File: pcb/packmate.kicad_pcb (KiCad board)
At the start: 2 copper layers, 77.2 x 93.3 mm, 49 parts, among them J2 DISPLAY, J7 MICROSD, Q1 2N7002E, SW1 BTN, SW2 Reset Button, SW3 Left Button, SW4 Right Button, SW6 Wireless On/Off Switch, U1 UP, U2 DWN, U3 LFT, U4 RHT

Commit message: Still tidying pcb design
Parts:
- removed C2: 0.1uf, Capacitor_SMD:C_01005_0402Metric
- added C10: 100nF, Capacitor_SMD:C_0402_1005Metric, B.Cu at (74.6, 70.3)
- added C11: 100nF, Capacitor_SMD:C_0402_1005Metric, B.Cu at (66.4, 114.6)
- added C12: 100nF, Capacitor_SMD:C_0402_1005Metric, B.Cu at (66.8, 127.0)
- added C13: 100nF, Capacitor_SMD:C_0402_1005Metric, B.Cu at (66.6, 140.1)
- added C14: 100nF, Capacitor_SMD:C_0402_1005Metric, B.Cu at (139.1, 127.3)
- added C15: 100nF, Capacitor_SMD:C_0402_1005Metric, B.Cu at (138.5, 115.9)
- added C16: 100nF, Capacitor_SMD:C_0402_1005Metric, B.Cu at (139.5, 104.5)
- added C17: 100nF, Capacitor_SMD:C_0402_1005Metric, B.Cu at (139.0, 79.2)
- added C18: 100nF, Capacitor_SMD:C_0402_1005Metric, B.Cu at (126.4, 69.6)
- added C9: 100nF, Capacitor_SMD:C_0402_1005Metric, B.Cu at (83.3, 66.1)
- added R13: 100, Resistor_SMD:R_0603_1608Metric, B.Cu at (116.9, 95.3)
- C1: footprint Capacitor_SMD:C_01005_0402Metric -> Capacitor_SMD:C_0402_1005Metric
- C3: value 400uf -> 100uf; footprint Capacitor_SMD:CP_Elec_3x5.3 -> Capacitor_SMD:CP_Elec_4x5.4
- C8: footprint Capacitor_SMD:C_01005_0402Metric -> Capacitor_SMD:C_0402_1005Metric; moved to B.Cu
- R10, R11, R12: footprint Resistor_SMD:R_0201_0603Metric -> Resistor_SMD:R_0603_1608Metric
- R9: value 10 -> 180; footprint Resistor_SMD:R_0201_0603Metric -> Resistor_SMD:R_0603_1608Metric
- moved R10 3.20 mm to (106.7, 91.5)
- moved R9 2.48 mm to (90.4, 92.9), turned to 180 degrees
- moved C8 1.82 mm to (86.0, 101.2)
- moved C1 1.27 mm to (99.7, 99.2), turned to 0 degrees
- moved R12 1.24 mm to (83.2, 101.5)
- moved Q1 1.22 mm to (108.1, 87.9), turned to -90 degrees
- moved D7 0.94 mm to (72.8, 74.5)
- moved R11 0.94 mm to (83.2, 98.6), turned to 0 degrees
- moved C3 0.30 mm to (88.9, 64.6)
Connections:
- net /3v3 renamed /3V3
- net /5v renamed /VSYS
- A1 pad 33: unconnected-(A1-AGND-Pad33) -> GND
- BZ1 pad 1: Net-(A1-GPIO12) -> Net-(BZ1-+)
- Q1 pad 2: Net-(Q1-S) -> /Display Connector/GND
- Q1 pad 3: /Display Connector/GND -> Net-(Q1-D)
- R10 pad 1: Net-(Q1-S) -> Net-(Q1-D)
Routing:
- net /Display Connector/GND: track 622.8 -> 111.7 mm, vias 9 -> 3
- net /VSYS: track 273.7 -> 284.4 mm
- net Net-(A1-RUN): track 121.6 -> 115.8 mm
- net Net-(BZ1-+): track 0.00 -> 5.64 mm
- net Net-(A1-GPIO12): track 8.73 -> 4.51 mm
- net /Display Connector/LEDK: track 8.69 -> 4.77 mm
- net Net-(A1-GPIO21): track 8.19 -> 5.13 mm
- net /3V3: track 195.9 -> 193.2 mm
- net Net-(Q1-D): track 0.00 -> 2.40 mm
- net Net-(A1-GPIO13): track 14.6 -> 16.2 mm
- net Net-(Q1-S): track 1.23 -> 0.00 mm
- net Net-(D5-A): track 2.26 -> 3.49 mm
- net /Display Connector/CS: track 22.2 -> 21.3 mm
- net /Display Connector/D/C: track 22.7 -> 21.7 mm
- net /Display Connector/SCL: track 17.2 -> 16.4 mm
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- added copper zone on B.Cu, net /Display Connector/GND
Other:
- outline, holes or cut-outs redrawn

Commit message: Still improving pcb, I learned what a fiducial is today
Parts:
- added REF**: Fiducial_1mm_Mask2mm, Fiducial:Fiducial_1mm_Mask2mm, F.Cu at (135.2, 72.0)
- added REF**: Fiducial_1mm_Mask2mm, Fiducial:Fiducial_1mm_Mask2mm, F.Cu at (73.5, 83.0)
- added REF**: Fiducial_1mm_Mask2mm, Fiducial:Fiducial_1mm_Mask2mm, F.Cu at (138.5, 131.8)
- added REF**: Fiducial_1mm_Mask2mm, Fiducial:Fiducial_1mm_Mask2mm, B.Cu at (73.5, 83.0)
- added REF**: Fiducial_1mm_Mask2mm, Fiducial:Fiducial_1mm_Mask2mm, B.Cu at (135.2, 72.0)
- added REF**: Fiducial_1mm_Mask2mm, Fiducial:Fiducial_1mm_Mask2mm, B.Cu at (138.5, 131.8)
- C8: moved to F.Cu
- moved SW3 8.08 mm to (88.0, 138.2), turned to 180 degrees
- moved C9 1.14 mm to (82.5, 65.2)
- moved C16 1.05 mm to (138.5, 104.8)
- moved C10 0.88 mm to (75.3, 69.8)
- moved C8 0.87 mm to (85.2, 100.8)
- moved C11 0.49 mm to (66.8, 114.2)
- moved C14 0.45 mm to (139.1, 127.8)
- moved Q1 0.32 mm to (107.8, 87.8)
- moved R10 0.18 mm to (106.8, 91.3)
- moved C3 0.18 mm to (88.8, 64.5)
- moved R12 0.11 mm to (83.2, 101.6)
- moved C1 0.06 mm to (99.8, 99.2)
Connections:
- net /3V3 renamed +3.3V
- net /VSYS renamed VSYS
- A1 pad 13: /Display Connector/GND -> GND
- A1 pad 17: Net-(A1-GPIO13) -> /Display Connector/LEDK
- A1 pad 18: /Display Connector/GND -> GND
- A1 pad 23: /Display Connector/GND -> GND
- A1 pad 28: /Display Connector/GND -> GND
- A1 pad 3: /Display Connector/GND -> GND
- A1 pad 38: /Display Connector/GND -> GND
- A1 pad 8: /Display Connector/GND -> GND
- BZ1 pad 2: /Display Connector/GND -> GND
- C1 pad 1: /Display Connector/GND -> GND
- C10 pad 1: /Display Connector/GND -> GND
- C11 pad 1: /Display Connector/GND -> GND
- C12 pad 1: /Display Connector/GND -> GND
- C13 pad 1: /Display Connector/GND -> GND
- C14 pad 1: /Display Connector/GND -> GND
- C15 pad 1: /Display Connector/GND -> GND
- C16 pad 1: /Display Connector/GND -> GND
- C17 pad 1: /Display Connector/GND -> GND
- C18 pad 1: /Display Connector/GND -> GND
- C3 pad 2: /Display Connector/GND -> GND
- C4 pad 2: /Display Connector/GND -> GND
- C5 pad 2: /Display Connector/GND -> GND
- C6 pad 2: /Display Connector/GND -> GND
- C7 pad 2: /Display Connector/GND -> GND
- C8 pad 1: /Display Connector/GND -> GND
- C9 pad 1: /Display Connector/GND -> GND
- D1 pad 1: /Display Connector/GND -> GND
- D10 pad 3: /Display Connector/GND -> GND
- D11 pad 3: /Display Connector/GND -> GND
- D12 pad 3: /Display Connector/GND -> GND
- D13 pad 3: /Display Connector/GND -> GND
- D14 pad 3: /Display Connector/GND -> GND
- D15 pad 3: /Display Connector/GND -> GND
- D2 pad 1: /Display Connector/GND -> GND
- D3 pad 1: /Display Connector/GND -> GND
- D4 pad 1: /Display Connector/GND -> GND
- D5 pad 1: /Display Connector/GND -> GND
- D6 pad 3: /Display Connector/GND -> GND
- D7 pad 3: /Display Connector/GND -> GND
- D8 pad 3: /Display Connector/GND -> GND
- D9 pad 3: /Display Connector/GND -> GND
- J2 pad 1: /Display Connector/GND -> GND
- J2 pad 12: /Display Connector/GND -> GND
- J2 pad 2: /Display Connector/LEDK -> Net-(J2-Pin_2)
- J2 pad 5: /Display Connector/GND -> GND
- J2 pad 6: /Display Connector/GND -> GND
- J2 pad MP: (no net) -> GND
- J7 pad 6: /Display Connector/GND -> GND
- Q1 pad 1: Net-(A1-GPIO13) -> /Display Connector/LEDK
- Q1 pad 2: /Display Connector/GND -> GND
- R10 pad 2: /Display Connector/LEDK -> Net-(J2-Pin_2)
- SW1 pad 1: /Display Connector/GND -> GND
- SW2 pad 1: /Display Connector/GND -> GND
- SW3 pad 1: /Display Connector/GND -> GND
- SW4 pad 1: /Display Connector/GND -> GND
- SW6 pad 1: /Display Connector/GND -> GND
- U1 pad 3: /Display Connector/GND -> GND
- U2 pad 3: /Display Connector/GND -> GND
- U3 pad 3: /Display Connector/GND -> GND
- U4 pad 3: /Display Connector/GND -> GND
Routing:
- net GND: track 0.00 -> 121.5 mm, vias 0 -> 5
- net /Display Connector/GND: track 111.7 -> 0.00 mm, vias 3 -> 0
- net Net-(A1-GPIO15): track 92.5 -> 75.2 mm
- net Net-(A1-GPIO13): track 16.2 -> 0.00 mm
- net /Display Connector/LEDK: track 4.77 -> 16.4 mm, vias 1 -> 0
- net VSYS: track 284.4 -> 289.6 mm
- net Net-(J2-Pin_2): track 0.00 -> 4.77 mm, vias 0 -> 1
- net Net-(A1-GPIO14): track 54.7 -> 50.4 mm
- net Net-(D7-DOUT): track 54.4 -> 55.1 mm
- net /Trackball/BTN: track 82.1 -> 82.8 mm
- net Net-(D10-DOUT): track 91.9 -> 92.5 mm
- added copper zone on B.Cu, net GND
- removed copper zone on B.Cu, net /Display Connector/GND

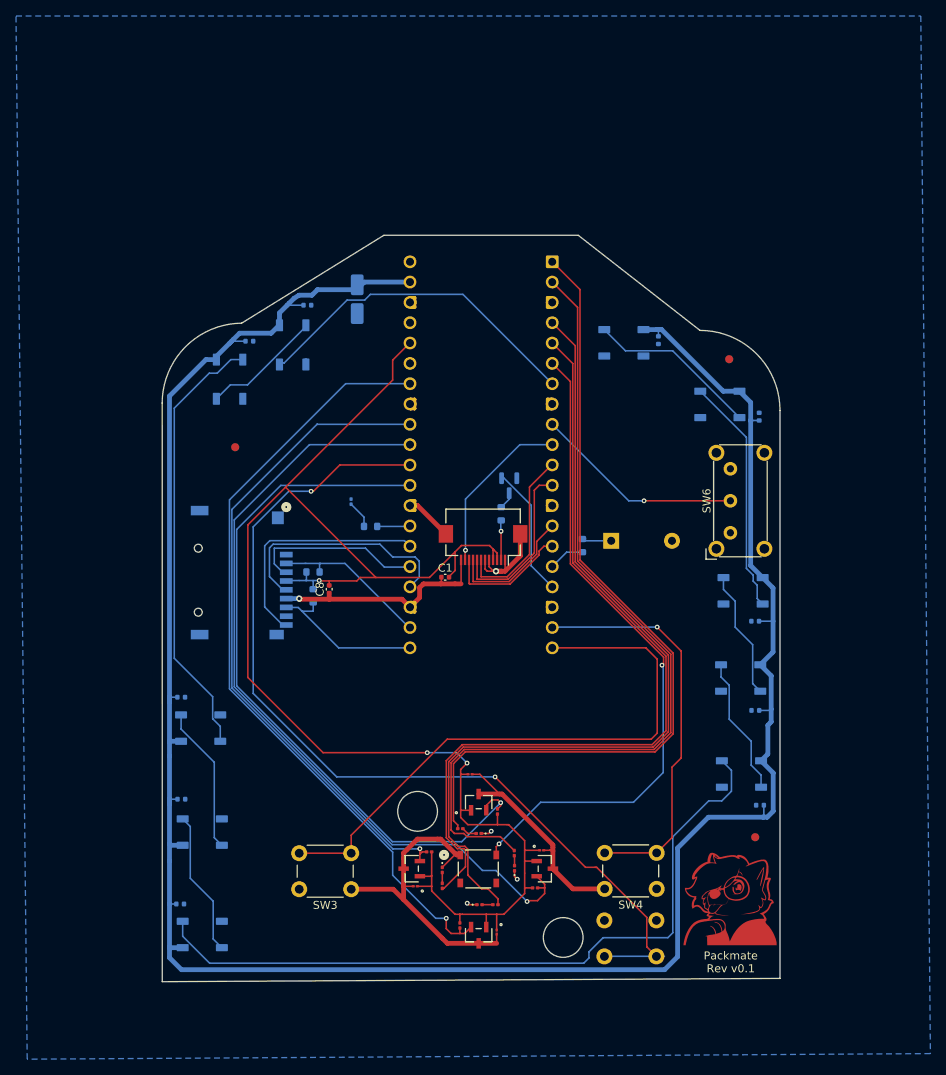
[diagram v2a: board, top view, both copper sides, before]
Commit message: I think the PCB is almost done for real this time chat. Just gotta add part numbers for the BOM
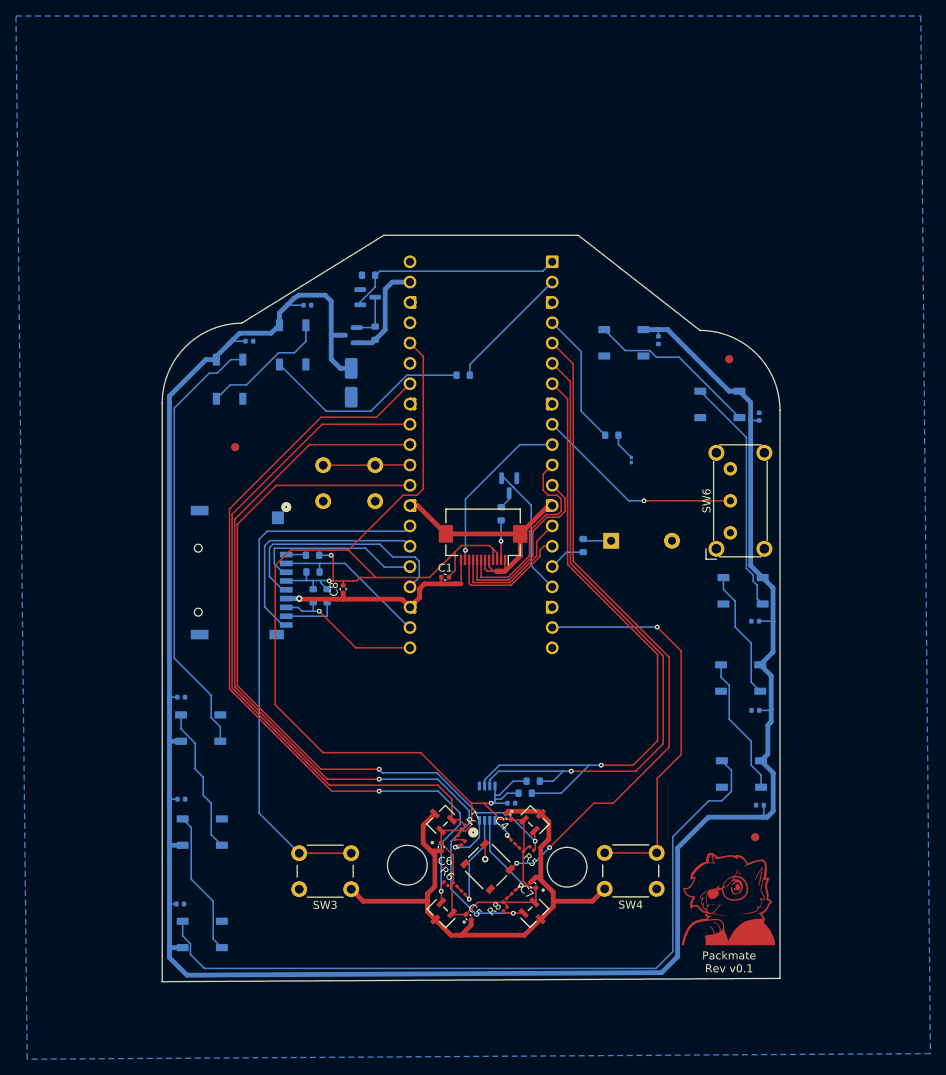
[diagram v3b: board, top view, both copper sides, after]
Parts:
- added C19: 0.1uf, Capacitor_SMD:C_0402_1005Metric, B.Cu at (108.0, 127.5)
- added Q2: AO3401A, Package_TO_SOT_SMD:SOT-23, B.Cu at (87.8, 69.0)
- added Q3: 2N7002E, Package_TO_SOT_SMD:SOT-23, B.Cu at (90.1, 64.2)
- added R14: 300, Resistor_SMD:R_0603_1608Metric, B.Cu at (102.0, 74.0)
- added R15: 10k, Resistor_SMD:R_0603_1608Metric, B.Cu at (83.2, 96.5)
- added R16: 10k, Resistor_SMD:R_0603_1608Metric, B.Cu at (85.0, 101.6)
- added R17: 100k, Resistor_SMD:R_0603_1608Metric, B.Cu at (91.0, 68.8)
- added R18: 100k, Resistor_SMD:R_0603_1608Metric, B.Cu at (90.2, 61.5)
- added R19: 4.7k, Resistor_SMD:R_0603_1608Metric, B.Cu at (110.8, 124.8)
- added R20: 4.7k, Resistor_SMD:R_0603_1608Metric, B.Cu at (109.8, 126.2)
- added U5: PCA9633DP1:PCA9633DP1, Package_SO:TSSOP-8_3x3mm_P0.65mm, B.Cu at (105.0, 127.5)
- C10, C11, C12, C13, C14, C15, C16, C17, C18, C9: value 100nF -> 0.1uf
- C4, C5, C6, C7: footprint Capacitor_SMD:C_01005_0402Metric -> Capacitor_SMD:C_0402_1005Metric
- D1: value BLU -> BLUE
- D3: value GRN -> GREEN
- D4: value WHT -> WHITE
- D5: value Wireless In Use LED -> YELLOW
- J2: value DISPLAY -> FH12-12S-0.5SH
- J7: value MICROSD -> MSD-4-A
- moved SW2 66.9 mm to (84.5, 89.8), turned to 0 degrees
- moved D5 35.4 mm to (123.0, 84.6), turned to 90 degrees
- moved R9 32.2 mm to (120.6, 81.5), turned to 0 degrees
- moved C3 10.5 mm to (88.0, 75.0)
- moved R2 8.09 mm to (109.3, 133.3), turned to -45 degrees
- moved U1 7.38 mm to (111.0, 129.6), turned to -45 degrees
- moved U3 7.15 mm to (99.2, 129.5), turned to 45 degrees
- moved C4 7.13 mm to (107.7, 129.2), turned to 135 degrees
- moved R3 6.32 mm to (101.1, 131.8), turned to 45 degrees
- moved R5 6.31 mm to (110.6, 133.2), turned to 135 degrees
- moved R4 5.99 mm to (107.2, 139.6), turned to -135 degrees
- moved C6 5.88 mm to (99.2, 133.0), turned to -90 degrees
- moved U4 5.73 mm to (110.9, 141.3), turned to -135 degrees
- moved R1 5.64 mm to (101.0, 137.7), turned to 135 degrees
- moved R6 5.51 mm to (99.9, 137.6), turned to -45 degrees
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- renumbered REF** to FID1, REF** to FID2, REF** to FID3, REF** to FID4, REF** to FID5, REF** to FID6
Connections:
- A1 pad 1: /Trackball/RED -> /RGB Matrix/LEDPower
- A1 pad 2: /Trackball/WHT -> /RGB Matrix/Data
- A1 pad 20: Net-(A1-GPIO15) -> unconnected-(A1-GPIO15-Pad20)
- A1 pad 37: /LiPo Shim/3E -> unconnected-(A1-3V3_EN-Pad37)
- A1 pad 4: /Trackball/BLU -> Net-(A1-GPIO2)
- A1 pad 40: /LiPo Shim/VB -> unconnected-(A1-VBUS-Pad40)
- A1 pad 5: /Trackball/GRN -> /Trackball/BTN
- A1 pad 6: /Trackball/BTN -> SDA0
- A1 pad 7: /RGB Matrix/Data -> SCL0
- C10 pad 2: VSYS -> Net-(D10-VDD)
- C11 pad 2: VSYS -> Net-(D10-VDD)
- C12 pad 2: VSYS -> Net-(D10-VDD)
- C13 pad 2: VSYS -> Net-(D10-VDD)
- C14 pad 2: VSYS -> Net-(D10-VDD)
- C15 pad 2: VSYS -> Net-(D10-VDD)
- C16 pad 2: VSYS -> Net-(D10-VDD)
- C17 pad 2: VSYS -> Net-(D10-VDD)
- C18 pad 2: VSYS -> Net-(D10-VDD)
- C3 pad 1: VSYS -> Net-(D10-VDD)
- C9 pad 2: VSYS -> Net-(D10-VDD)
- D1 pad 1: GND -> Net-(D1-K)
- D10 pad 1: VSYS -> Net-(D10-VDD)
- D11 pad 1: VSYS -> Net-(D10-VDD)
- D12 pad 1: VSYS -> Net-(D10-VDD)
- D13 pad 1: VSYS -> Net-(D10-VDD)
- D14 pad 1: VSYS -> Net-(D10-VDD)
- D15 pad 1: VSYS -> Net-(D10-VDD)
- D2 pad 1: GND -> Net-(D2-K)
- D3 pad 1: GND -> Net-(D3-K)
- D4 pad 1: GND -> Net-(D4-K)
- D6 pad 1: VSYS -> Net-(D10-VDD)
- D6 pad 4: /RGB Matrix/Data -> Net-(D6-DIN)
- D7 pad 1: VSYS -> Net-(D10-VDD)
- D8 pad 1: VSYS -> Net-(D10-VDD)
- D9 pad 1: VSYS -> Net-(D10-VDD)
- J7 pad 1: unconnected-(J7-DAT2-Pad1) -> Net-(J7-DAT2)
- J7 pad 8: unconnected-(J7-DAT1-Pad8) -> Net-(J7-DAT1)
- R1 pad 2: /Trackball/BLU -> +3.3V
- R2 pad 2: /Trackball/RED -> +3.3V
- R3 pad 2: /Trackball/GRN -> +3.3V
- R4 pad 2: /Trackball/WHT -> +3.3V
- R9 pad 1: Net-(A1-GPIO21) -> Net-(A1-GPIO2)
- SW3 pad 2: Net-(A1-GPIO15) -> Net-(A1-GPIO21)
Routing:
- net Net-(D10-VDD): track 0.00 -> 291.3 mm
- net VSYS: track 289.6 -> 12.8 mm
- net /Trackball/WHT: track 109.0 -> 0.00 mm
- net /Trackball/BLU: track 107.6 -> 0.00 mm
- net Net-(A1-RUN): track 116.3 -> 10.9 mm, vias 2 -> 0
- net /Trackball/RED: track 102.6 -> 0.00 mm
- net /Trackball/GRN: track 102.1 -> 0.00 mm
- net SCL0: track 0.00 -> 83.2 mm, vias 0 -> 1
- net SDA0: track 0.00 -> 81.0 mm, vias 0 -> 1
- net Net-(A1-GPIO15): track 75.2 -> 0.00 mm
- net Net-(A1-GPIO21): track 5.13 -> 68.4 mm
- net /RGB Matrix/LEDPower: track 0.00 -> 27.3 mm
- net Net-(D6-DIN): track 0.00 -> 26.4 mm
- net /RGB Matrix/Data: track 42.4 -> 16.0 mm
- net GND: track 121.5 -> 138.4 mm, vias 5 -> 2
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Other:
- outline, holes or cut-outs redrawn

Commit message: Fixing microsd card slot 3d model
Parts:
- moved C13 8.75 mm to (74.7, 136.8)
- moved D10 7.34 mm to (75.8, 140.2)
- moved D9 1.80 mm to (71.2, 130.8)
- moved C12 1.75 mm to (68.5, 127.1)
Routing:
- net Net-(D10-DOUT): track 94.8 -> 89.8 mm
- net Net-(D10-VDD): track 291.3 -> 287.2 mm
- net Net-(D10-DIN): track 18.1 -> 20.0 mm
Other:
- board size 77.2 x 93.3 mm -> 77.2 x 92.9 mm

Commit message: I think the PCB is ready to ship, just gonna tidy up a couple more things
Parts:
- BZ1: footprint Buzzer_Beeper:Buzzer_12x9.5RM7.6 -> Buzzer_Beeper:Buzzer_TDK_PS1240P02BT_D12.2mm_H6.5mm
- C3: footprint Capacitor_SMD:CP_Elec_4x5.4 -> Capacitor_SMD:C_1206_3216Metric
- D1, D2, D3, D4, D5: footprint LED_SMD:LED_0201_0603Metric -> LED_SMD:LED_0402_1005Metric
- J2: value FH12-12S-0.5SH -> FFC2B28-12-G; footprint Connector_FFC-FPC:Hirose_FH12-12S-0.5SH_1x12-1MP_P0.50mm_Horizontal -> FFC2B28-12-G:GCT_FFC2B28-12-G
- R14: moved to F.Cu
- R2: value 180 -> 360
- R3: value 180 -> 330
- U1: value UP -> TMAG5231C1GQDBZR
- U2: value DWN -> TMAG5231C1GQDBZR
- U3: value LFT -> TMAG5231C1GQDBZR
- U4: value RHT -> TMAG5231C1GQDBZR
- U5: value PCA9633DP1:PCA9633DP1 -> PCA9633DP1
- moved C1 27.8 mm to (99.2, 71.5), turned to -90 degrees
- moved J2 25.0 mm to (104.2, 70.2), turned to 0 degrees
- moved R14 20.6 mm to (81.4, 75.2)
- moved R10 15.3 mm to (103.0, 76.5), turned to 90 degrees
- moved Q1 9.35 mm to (104.5, 79.1), turned to 90 degrees
- moved D5 8.01 mm to (130.7, 82.2), turned to 180 degrees
- moved R9 7.64 mm to (128.2, 82.2)
- moved R1 3.30 mm to (104.0, 139.0), turned to 45 degrees
- moved R3 2.00 mm to (101.2, 133.8), turned to -45 degrees
- moved BZ1 1.75 mm to (122.2, 94.7)
- moved R7 1.42 mm to (102.0, 129.1), turned to -90 degrees
- moved R2 0.88 mm to (108.5, 133.8), turned to -135 degrees
- moved R4 0.65 mm to (107.0, 139.0), turned to 135 degrees
- moved D1 0.26 mm to (102.2, 138.8), turned to -45 degrees
- moved D2 0.23 mm to (108.0, 132.2)
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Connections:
- R1 pad 2: +3.3V -> VSYS
- R2 pad 2: +3.3V -> VSYS
- R3 pad 2: +3.3V -> VSYS
- R4 pad 2: +3.3V -> VSYS
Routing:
- net VSYS: track 12.8 -> 163.9 mm, vias 0 -> 2
- net /RGB Matrix/Data: track 16.0 -> 38.9 mm
- net Net-(D6-DIN): track 26.4 -> 3.62 mm, vias 0 -> 1
- net GND: track 138.4 -> 116.8 mm, vias 2 -> 3
- net /Display Connector/SDA: track 15.9 -> 33.0 mm
- net /Display Connector/SCL: track 16.7 -> 31.5 mm
- net /Display Connector/LEDK: track 16.4 -> 23.7 mm, vias 0 -> 1
- net +3.3V: track 201.5 -> 194.6 mm
- net /Display Connector/CS: track 22.8 -> 27.5 mm
- net Net-(A1-GPIO2): track 16.9 -> 21.6 mm, vias 0 -> 1
- net /Display Connector/RST: track 21.3 -> 18.5 mm
- net Net-(D3-K): track 6.55 -> 4.19 mm
- net Net-(J2-Pad2): track 4.77 -> 7.11 mm
- net Net-(D5-A): track 3.49 -> 1.19 mm
- net Net-(D1-K): track 11.4 -> 10.0 mm
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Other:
- board text added: "PICO PLUS 2W"
- board text added: "USBC"
